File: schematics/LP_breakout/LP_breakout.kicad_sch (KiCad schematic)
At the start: 8 parts, among them J1 RJ45, J2 Conn_01x03_Socket, J3 Conn_02x04_Odd_Even, J4 Conn_02x15_Odd_Even, J5 Conn_02x02_Odd_Even, J6 Conn_01x03_Socket, J7 Conn_01x03_Socket, J8 Conn_01x03_Socket

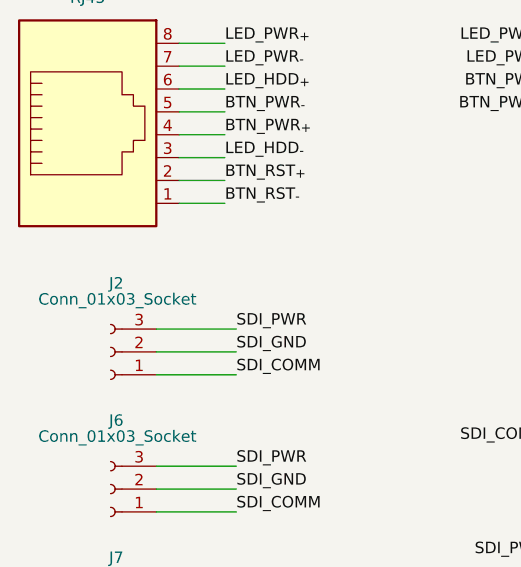
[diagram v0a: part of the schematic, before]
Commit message: Added regulators to Shunt_Link, Edited lib
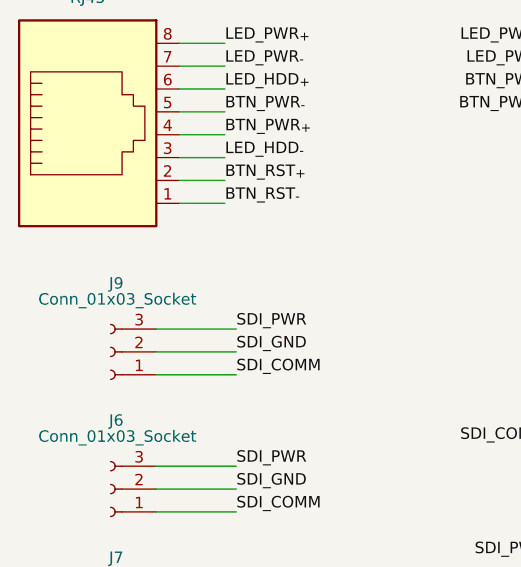
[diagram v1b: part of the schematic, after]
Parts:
- renumbered J2 to J9
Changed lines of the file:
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@@
 		(on_board yes)
 		(dnp no)
-		(property "Reference" "J2"
+		(property "Reference" "J9"
 			(at 36.195 54.61 0)
 			(effects
@@
 			(project ""
 				(path "/80ae3edd-3088-4067-bc99-625be8dfe1e2"
-					(reference "J2")
+					(reference "J9")
 					(unit 1)
 				)

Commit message: Update libraries to one lib for all projects
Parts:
- J6, J7, J8, J9: footprint Library:MC1,5_3-G-3,5 -> Link_Footprints:PC-1844223
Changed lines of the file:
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@@
 			)
 		)
-		(property "Footprint" "Library:MC1,5_3-G-3,5"
+		(property "Footprint" "Link_Footprints:PC-1844223"
 			(at 35.56 106.68 0)
 			(effects
@@
 			)
 		)
-		(property "Footprint" "Library:MC1,5_3-G-3,5"
+		(property "Footprint" "Link_Footprints:PC-1844223"
 			(at 35.56 92.71 0)
 			(effects
@@
 			)
 		)
-		(property "Footprint" "Library:MC1,5_3-G-3,5"
+		(property "Footprint" "Link_Footprints:PC-1844223"
 			(at 35.56 62.23 0)
 			(effects
@@
 			)
 		)
-		(property "Footprint" "Library:MC1,5_3-G-3,5"
+		(property "Footprint" "Link_Footprints:PC-1844223"
 			(at 35.56 77.47 0)
 			(effects
